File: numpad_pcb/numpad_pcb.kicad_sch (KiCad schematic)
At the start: 21 parts, among them J1 numpad, U1 ProMicro

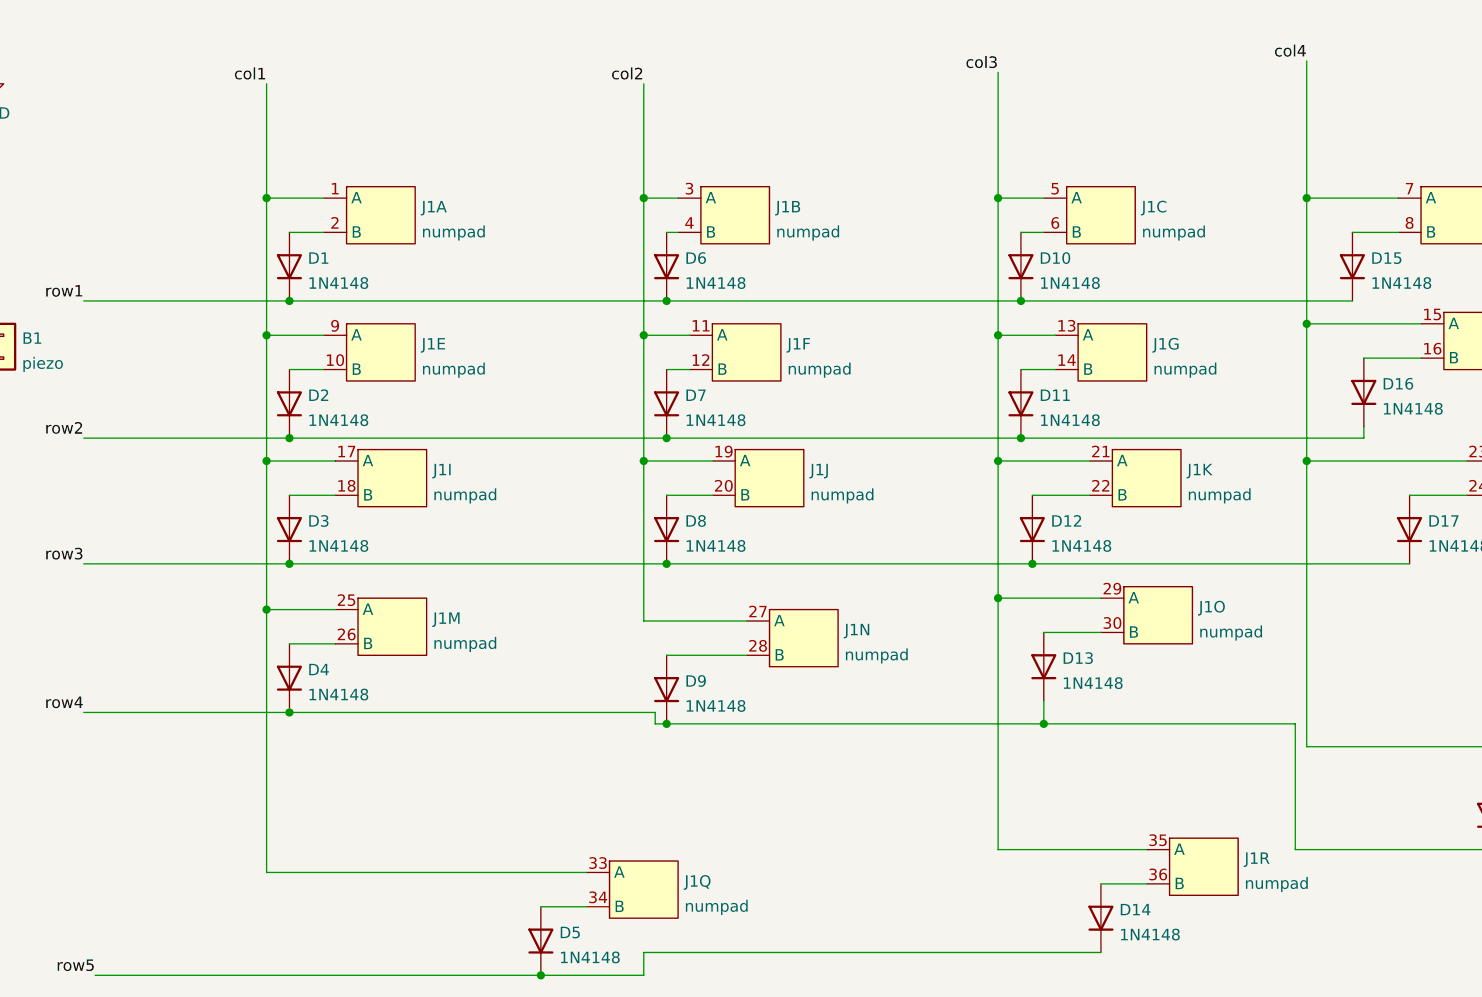
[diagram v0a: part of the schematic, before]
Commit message: fixed layout to allow for remapping to adm3a pinout
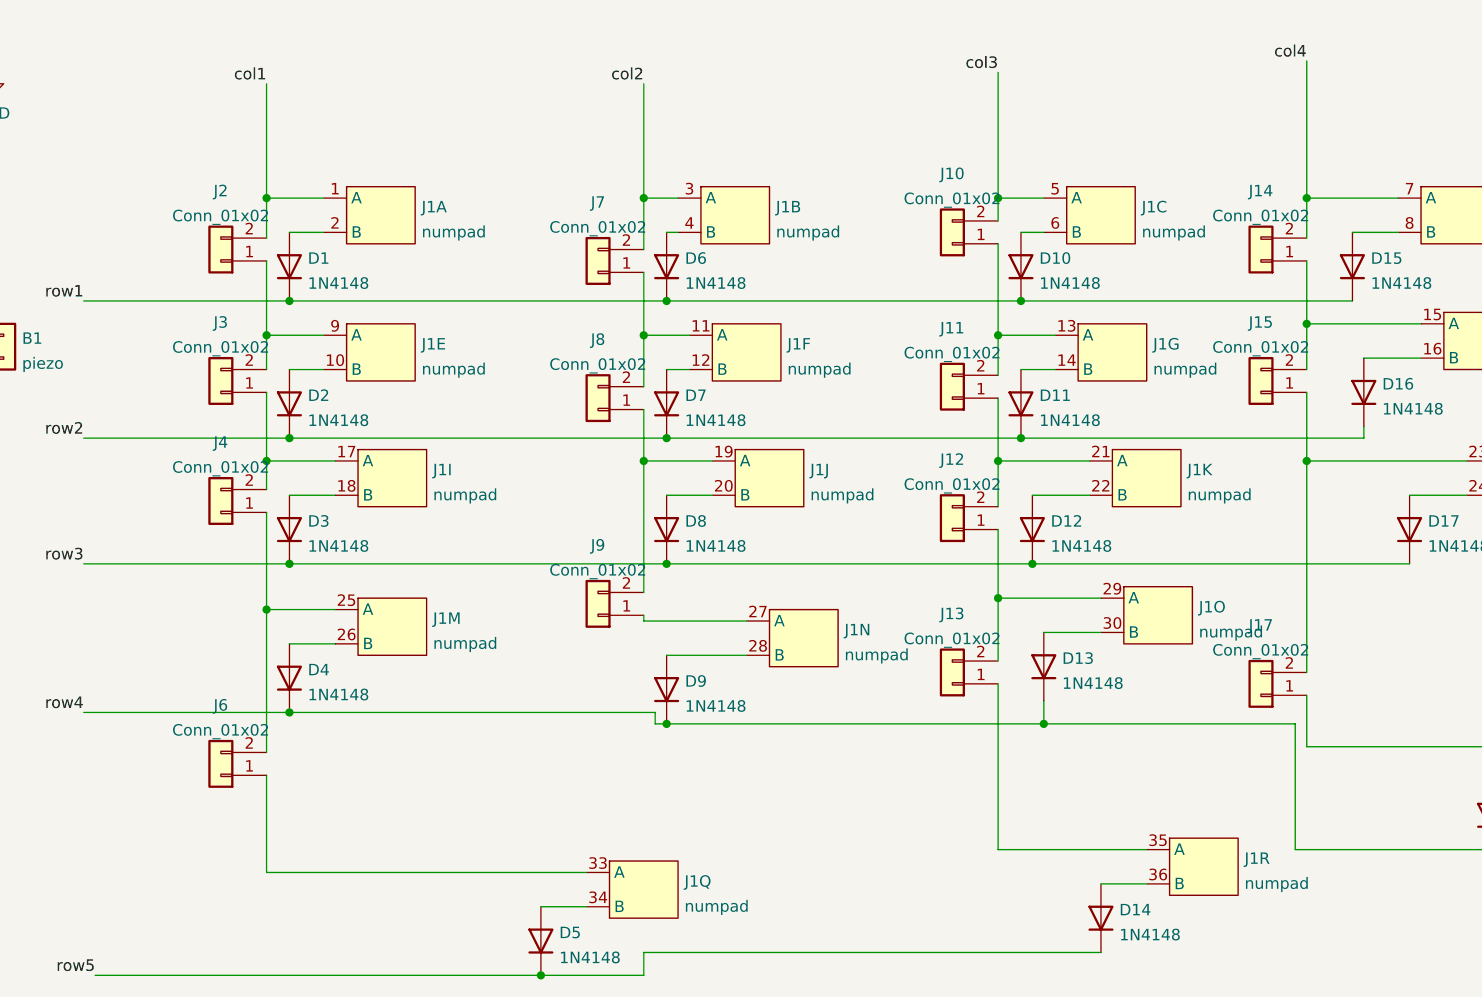
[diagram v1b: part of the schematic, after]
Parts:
- added J10, J11, J12, J13, J14, J15, J17, J2, J3, J4, J6, J7, J8, J9: Conn_01x02, Jumper:SolderJumper-2_P1.3mm_Open_TrianglePad1.0x1.5mm, symbol Connector_Generic:Conn_01x02
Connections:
- net col1: now also J2.2 (Pin_2); no longer J1.17 (A), J1.25 (A), J1.33 (A), J1.9 (A)
- net col2: now also J7.2 (Pin_2); no longer J1.11 (A), J1.19 (A), J1.27 (A)
- net col3: now also J10.2 (Pin_2); no longer J1.13 (A), J1.21 (A), J1.29 (A), J1.35 (A)
- net col4: now also J14.2 (Pin_2); no longer J1.15 (A), J1.23 (A), J1.31 (A)
- new net: J1.25 (A), J4.1 (Pin_1), J6.2 (Pin_2)
- new net: J1.9 (A), J2.1 (Pin_1), J3.2 (Pin_2)
- new net: J1.11 (A), J7.1 (Pin_1), J8.2 (Pin_2)
- new net: J1.35 (A), J13.1 (Pin_1)
- new net: J1.29 (A), J12.1 (Pin_1), J13.2 (Pin_2)
- new net: J1.13 (A), J10.1 (Pin_1), J11.2 (Pin_2)
- new net: J1.15 (A), J14.1 (Pin_1), J15.2 (Pin_2)
- new net: J1.31 (A), J17.1 (Pin_1)
- new net: J1.23 (A), J15.1 (Pin_1), J17.2 (Pin_2)
- new net: J1.21 (A), J11.1 (Pin_1), J12.2 (Pin_2)
- new net: J1.17 (A), J3.1 (Pin_1), J4.2 (Pin_2)
- new net: J1.19 (A), J8.1 (Pin_1), J9.2 (Pin_2)
- new net: J1.27 (A), J9.1 (Pin_1)
- new net: J1.33 (A), J6.1 (Pin_1)

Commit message: tweaked silk, added todo for upgraded layout, added config
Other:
- note added: "TODO: move all jumpers to back of board add jumpers for rows in addition to columns"
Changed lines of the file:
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@@
+    (stroke (width 0) (type default) (color 0 0 0 0))
+  )
+  (polyline (pts (xy 34.925 147.32) (xy 34.925 191.77))
     (stroke (width 0) (type default) (color 0 0 0 0))
   )
@@
     (stroke (width 0) (type default) (color 0 0 0 0))
   )
+  (polyline (pts (xy 34.925 147.32) (xy 162.56 147.32))
+    (stroke (width 0) (type default) (color 0 0 0 0))
+  )
   (wire (pts (xy 212.09 105.41) (xy 236.22 105.41))
     (stroke (width 0) (type default) (color 0 0 0 0))
@@
     (stroke (width 0) (type default) (color 0 0 0 0))
   )
+  (polyline (pts (xy 162.56 147.32) (xy 162.56 191.77))
+    (stroke (width 0) (type default) (color 0 0 0 0))
+  )
   (wire (pts (xy 212.09 44.45) (xy 212.09 48.895))
     (stroke (width 0) (type default) (color 0 0 0 0))
@@
     (stroke (width 0) (type default) (color 0 0 0 0))
   )
+  (polyline (pts (xy 162.56 191.77) (xy 34.925 191.77))
+    (stroke (width 0) (type default) (color 0 0 0 0))
+  )
   (wire (pts (xy 96.52 44.45) (xy 96.52 48.895))
     (stroke (width 0) (type default) (color 0 0 0 0))
@@
     (stroke (width 0) (type default) (color 0 0 0 0))
   )
+  (text "TODO:\nmove all jumpers to back of board\nadd jumpers for rows in addition to columns"
+    (at 74.295 172.085 0)
+    (effects (font (size 1.27 1.27)) (justify left bottom))
+  )
   (label "row2" (at 76.2 71.12 180)

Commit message: tweaked schematic
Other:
- note added: "TODO: move all jumpers to back of board"
- note removed: "TODO: move all jumpers to back of board add jumpers for rows in addition to columns"
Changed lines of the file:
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@@
     (stroke (width 0) (type default) (color 0 0 0 0))
   )
-  (text "TODO:\nmove all jumpers to back of board\nadd jumpers for rows in addition to columns"
-    (at 74.295 172.085 0)
+  (text "TODO:\nmove all jumpers to back of board" (at 74.295 172.085 0)
     (effects (font (size 1.27 1.27)) (justify left bottom))
   )

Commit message: moved jumpers to the back
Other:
- note removed: "TODO: move all jumpers to back of board"
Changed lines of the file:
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@@
-    (stroke (width 0) (type default) (color 0 0 0 0))
-  )
-  (polyline (pts (xy 34.925 147.32) (xy 34.925 191.77))
     (stroke (width 0) (type default) (color 0 0 0 0))
   )
@@
     (stroke (width 0) (type default) (color 0 0 0 0))
   )
-  (polyline (pts (xy 34.925 147.32) (xy 162.56 147.32))
-    (stroke (width 0) (type default) (color 0 0 0 0))
-  )
   (wire (pts (xy 212.09 105.41) (xy 236.22 105.41))
     (stroke (width 0) (type default) (color 0 0 0 0))
@@
     (stroke (width 0) (type default) (color 0 0 0 0))
   )
-  (polyline (pts (xy 162.56 147.32) (xy 162.56 191.77))
-    (stroke (width 0) (type default) (color 0 0 0 0))
-  )
   (wire (pts (xy 212.09 44.45) (xy 212.09 48.895))
     (stroke (width 0) (type default) (color 0 0 0 0))
@@
     (stroke (width 0) (type default) (color 0 0 0 0))
   )
-  (polyline (pts (xy 162.56 191.77) (xy 34.925 191.77))
-    (stroke (width 0) (type default) (color 0 0 0 0))
-  )
   (wire (pts (xy 96.52 44.45) (xy 96.52 48.895))
     (stroke (width 0) (type default) (color 0 0 0 0))
@@
     (stroke (width 0) (type default) (color 0 0 0 0))
   )
-  (text "TODO:\nmove all jumpers to back of board" (at 74.295 172.085 0)
-    (effects (font (size 1.27 1.27)) (justify left bottom))
-  )
   (label "row2" (at 76.2 71.12 180)
